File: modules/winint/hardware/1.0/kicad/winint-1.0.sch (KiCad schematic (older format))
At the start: 65 parts, among them J1 Screw_Terminal_01x09, J2 Screw_Terminal_01x09, J3 M12-5PIN, J4 RELAYS, K1 SANYOU_SRD_Form_C, K2 SANYOU_SRD_Form_C, Q1 2N2219, Q2 2N2219, SW1 INSTANCE, U1 ROT, U2 DOK, U3 STP, U4 DEP, U5 RET, U6 OVL, U7 Teensy_3.2, U8 TEC2-2411WI, U9 MCP2551-I-P

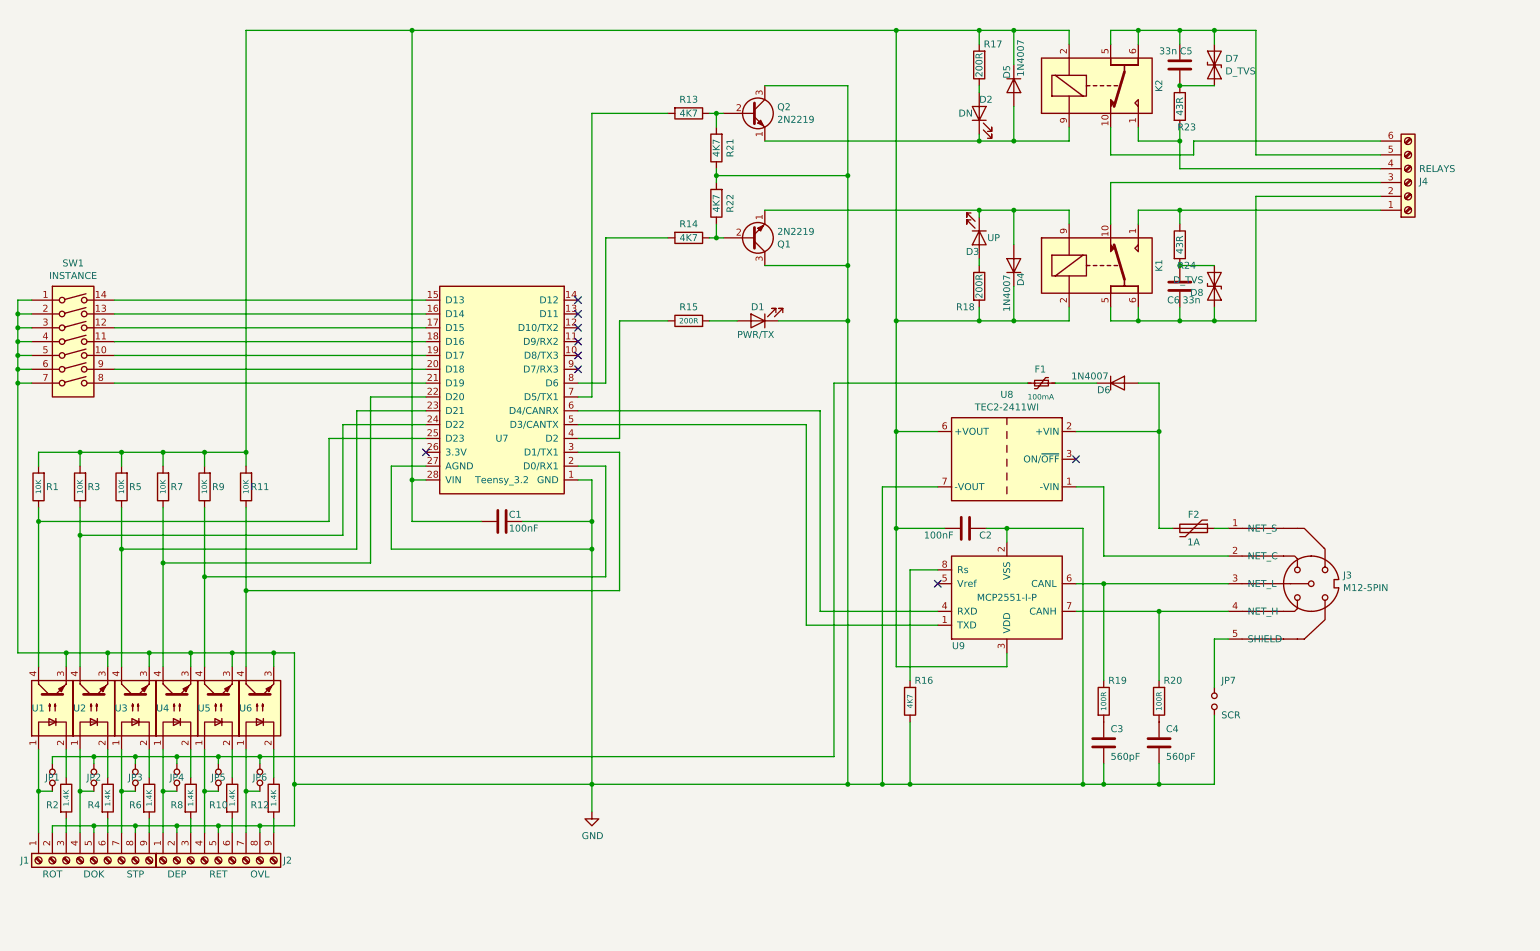
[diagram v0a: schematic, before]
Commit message: Revised PCB layout
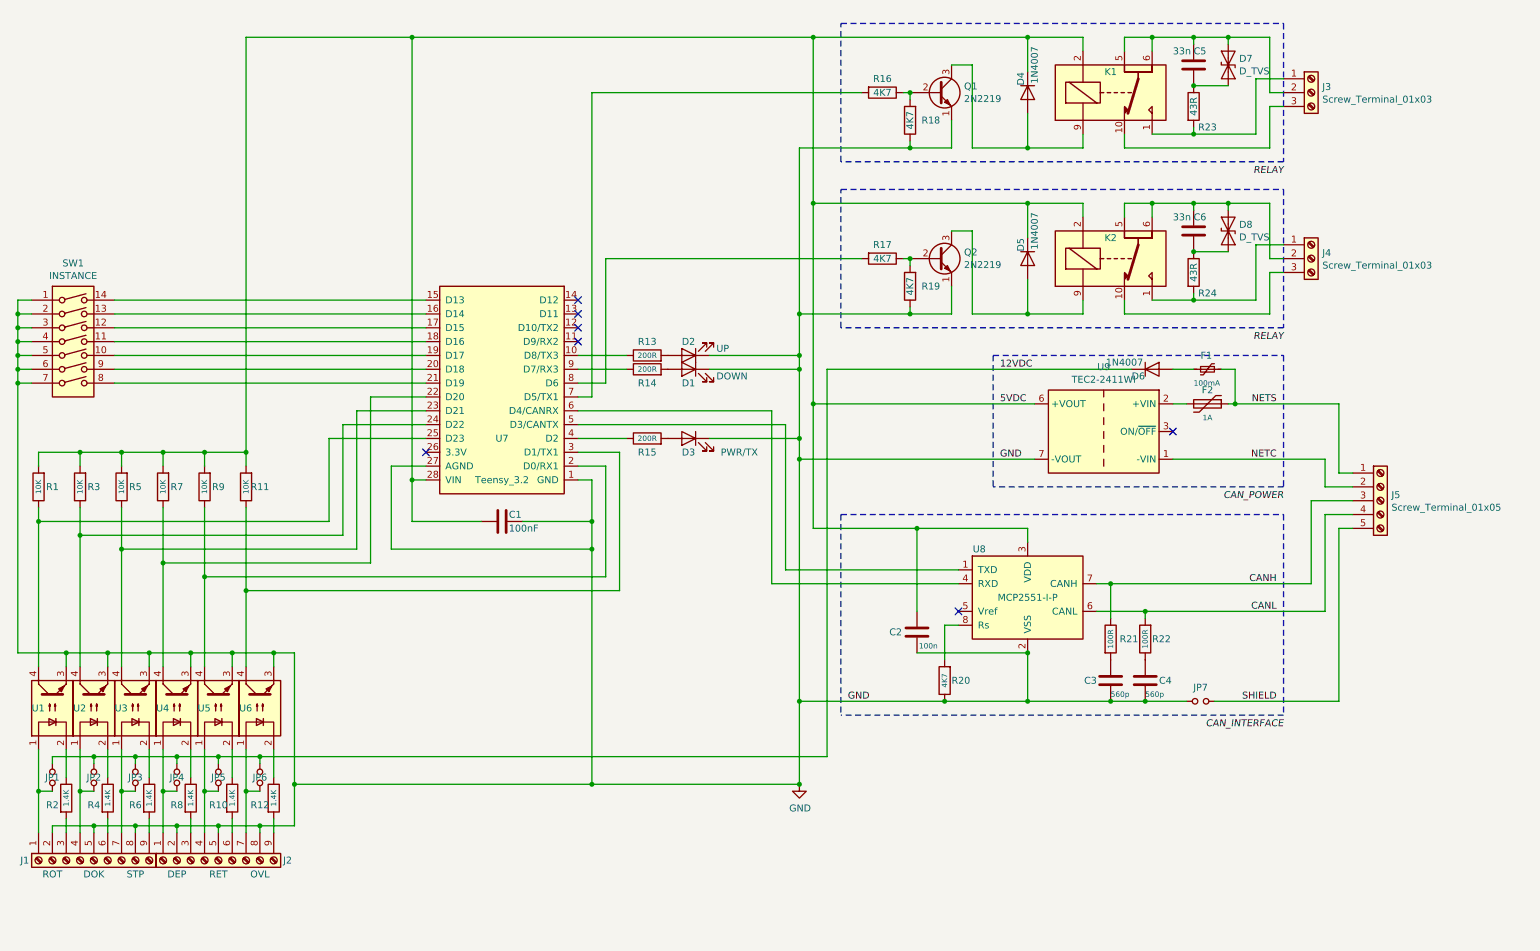
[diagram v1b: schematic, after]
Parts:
- removed D3: UP, LED_THT:LED_D3.0mm, symbol Device:LED
- removed D4: 1N4007, Diode_THT:D_DO-41_SOD81_P7.62mm_Horizontal, symbol Diode:1N4007
- removed J3: M12-5PIN, TerminalBlock_Phoenix:TerminalBlock_Phoenix_MPT-0,5-5-2.54_1x05_P2.54mm_Horizontal, symbol pdjr:M12-5PIN
- removed J4: RELAYS, TerminalBlock_Phoenix:TerminalBlock_Phoenix_MPT-0,5-6-2.54_1x06_P2.54mm_Horizontal, symbol Connector:Screw_Terminal_01x06
- removed R21, R22: 4K7, Resistor_THT:R_Axial_DIN0204_L3.6mm_D1.6mm_P5.08mm_Horizontal, symbol Device:R
- added D1: DOWN, LED_THT:LED_D3.0mm, symbol Device:LED
- added D5: 1N4007, Diode_THT:D_DO-34_SOD68_P2.54mm_Vertical_AnodeUp, symbol Diode:1N4007
- added J3, J4: Screw_Terminal_01x03, TerminalBlock_Phoenix:TerminalBlock_Phoenix_MPT-0,5-3-2.54_1x03_P2.54mm_Horizontal, symbol Connector:Screw_Terminal_01x03
- added J5: Screw_Terminal_01x05, TerminalBlock_Phoenix:TerminalBlock_Phoenix_MPT-0,5-5-2.54_1x05_P2.54mm_Horizontal, symbol Connector:Screw_Terminal_01x05
- added R16, R19: 4K7, Resistor_THT:R_Axial_DIN0204_L3.6mm_D1.6mm_P5.08mm_Horizontal, symbol Device:R
- C2: value 100nF -> 100n
- C3, C4: value 560pF -> 560p
- D2: value DN -> UP
- D4: renamed from D5; footprint Diode_THT:D_DO-41_SOD81_P7.62mm_Horizontal -> Diode_THT:D_DO-34_SOD68_P2.54mm_Vertical_AnodeUp
- K1, K2: footprint PDJR:RS_RELAY_476-757 -> PDJR:476-257
- Q1, Q2: footprint Package_TO_SOT_THT:TO-39-3 -> Package_TO_SOT_THT:TO-18-3
- R13, R14: value 4K7 -> 200R; Power (none) -> 0.125W
- R17, R18: value 200R -> 4K7; Power 0.125W -> (none)
- renumbered D1 to D3, R16 to R20, R19 to R21, R20 to R22, U9 to U8, U8 to U9
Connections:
- net GND: now also D2.1 (K), JP7.2, Q1.1 (E), Q2.1 (E), R18.1, D1.1 (K), R19.1; no longer JP7.1, Q1.3 (C), Q2.3 (C)
- net 5VDC: now reaches C1.1, C2.1, D4.1 (K), K1.2, K2.2, R1.2, R11.2, R3.2, R5.2, R7.2, R9.2, U7.28 (VIN), U8.3 (VDD), U9.6 (+VOUT)
- net 5VDC: now also D5.1 (K); no longer R17.2, R18.2
- net CANH: now reaches R21.1
- net CANH: now also U8.7 (CANH), J5.3 (Pin_3); no longer U8.6 (CANL)
- net CANL: now reaches R22.2
- net CANL: now also U8.6 (CANL), J5.4 (Pin_4); no longer U8.7 (CANH)
- net 12VDC: now reaches D6.1 (K)
- net 12VDC: now also JP1.2, JP2.2, JP3.2, JP4.2, JP5.2, JP6.2; no longer F1.1
- net at K1.9: now also D4.2 (A), Q1.3 (C); no longer Q1.1 (E)
- net at R14.1: now also U7.9 (D7/RX3); no longer Q1.2 (B)
- net at R13.1: now also U7.10 (D8/TX3); no longer Q2.2 (B)
- net at U7.7 (D5/TX1): now also R16.2; no longer R13.2
- net at K1.1: now also R23.2, J3.1 (Pin_1); no longer R24.1
- net at K1.5, K1.6: now also C5.2, D7.1 (A1), J3.2 (Pin_2); no longer C6.2, D8.1 (A1)
- net at K1.10: now also J3.3 (Pin_3)
- net at K2.1: now also R24.2, J4.1 (Pin_1); no longer R23.2
- net at K2.5, K2.6: now also C6.2, D8.1 (A1), J4.2 (Pin_2); no longer C5.2, D7.1 (A1)
- net at K2.10: now also J4.3 (Pin_3)
- net at U7.8 (D6): now also R17.2; no longer R14.2
- net at R17.1: now also Q2.2 (B), R19.2; no longer D2.2 (A)
- net NETS: now reaches F2.1
- net NETS: now also F1.1, J5.1 (Pin_1)
- net at F2.2, U9.2 (+VIN): no longer D6.2 (A)
- net NETC: now reaches U9.1 (-VIN)
- net NETC: now also J5.2 (Pin_2)
- net at C6.1, D8.2 (A2): now also R24.1; no longer R24.2
- new net: D6.2 (A), F1.2
- new net: Q1.2 (B), R16.1, R18.2
- new net: D5.2 (A), K2.9, Q2.3 (C)
- new net: D1.2 (A), R14.2
- new net: D2.2 (A), R13.2
- new net SHIELD: J5.5 (Pin_5), JP7.1
- no-connect marks 9 -> 7
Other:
- moved on the sheet: C2, C3, C4, C5, D3, D4, D6, D7, F1, F2, JP7, R15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

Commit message: Revised PCB layout
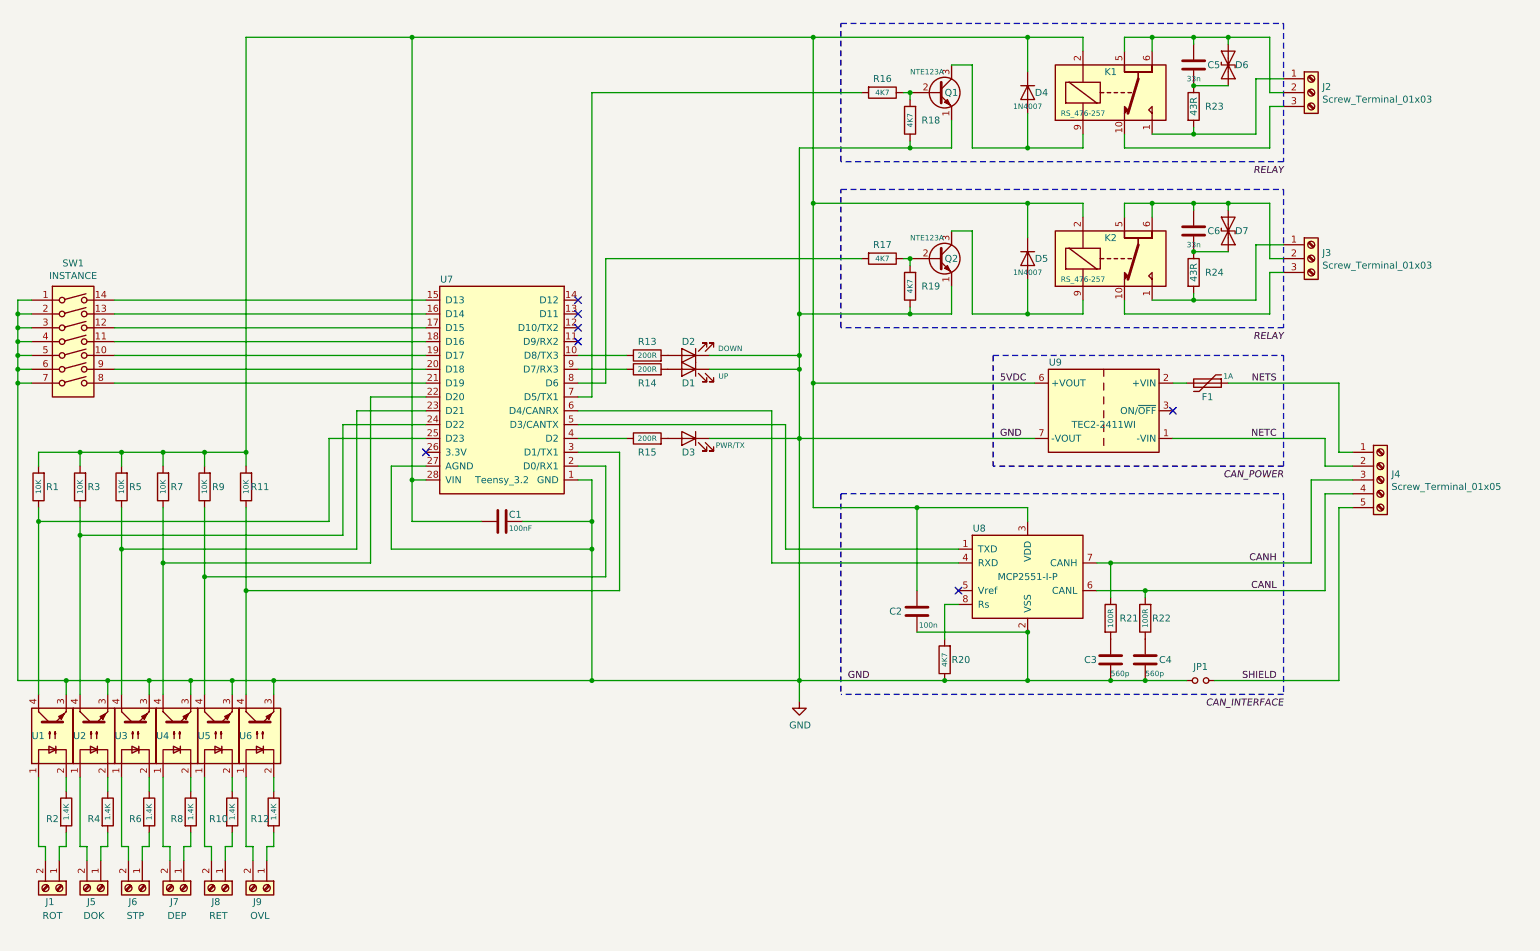
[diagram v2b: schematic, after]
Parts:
- removed D6: 1N4007, Diode_THT:D_DO-41_SOD81_P7.62mm_Horizontal, symbol Diode:1N4007
- removed F1: 100mA, Fuse:Fuse_Littelfuse_395Series, symbol Device:Polyfuse_Small
- removed J1, J2: Screw_Terminal_01x09, TerminalBlock_Phoenix:TerminalBlock_Phoenix_MPT-0,5-9-2.54_1x09_P2.54mm_Horizontal, symbol Connector:Screw_Terminal_01x09
- removed JP1, JP2, JP3, JP4, JP5, JP6: SCR, Connector_PinHeader_2.54mm:PinHeader_1x02_P2.54mm_Vertical, symbol Device:Jumper_NO_Small
- added J1: ROT, TerminalBlock_Phoenix:TerminalBlock_Phoenix_MPT-0,5-2-2.54_1x02_P2.54mm_Horizontal, symbol Connector:Screw_Terminal_01x02
- added J5: DOK, TerminalBlock_Phoenix:TerminalBlock_Phoenix_MPT-0,5-2-2.54_1x02_P2.54mm_Horizontal, symbol Connector:Screw_Terminal_01x02
- added J6: STP, TerminalBlock_Phoenix:TerminalBlock_Phoenix_MPT-0,5-2-2.54_1x02_P2.54mm_Horizontal, symbol Connector:Screw_Terminal_01x02
- added J7: DEP, TerminalBlock_Phoenix:TerminalBlock_Phoenix_MPT-0,5-2-2.54_1x02_P2.54mm_Horizontal, symbol Connector:Screw_Terminal_01x02
- added J8: RET, TerminalBlock_Phoenix:TerminalBlock_Phoenix_MPT-0,5-2-2.54_1x02_P2.54mm_Horizontal, symbol Connector:Screw_Terminal_01x02
- added J9: OVL, TerminalBlock_Phoenix:TerminalBlock_Phoenix_MPT-0,5-2-2.54_1x02_P2.54mm_Horizontal, symbol Connector:Screw_Terminal_01x02
- K1, K2: value SANYOU_SRD_Form_C -> RS_476-257
- Q1, Q2: value 2N2219 -> NTE123A
- renumbered D2 to D1, D1 to D2, D7 to D6, D8 to D7, F2 to F1, J3 to J2, J4 to J3, J5 to J4, JP7 to JP1
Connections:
- net at U1.1: now also J1.2 (Pin_2)
- net at R2.2: now also J1.1 (Pin_1)
- net at U2.1: now also J5.2 (Pin_2)
- net at R4.2: now also J5.1 (Pin_1)
- net at U3.1: now also J6.2 (Pin_2)
- net at R6.2: now also J6.1 (Pin_1)
- net at U4.1: now also J7.2 (Pin_2)
- net at R8.2: now also J7.1 (Pin_1)
- net at U5.1: now also J8.2 (Pin_2)
- net at R10.2: now also J8.1 (Pin_1)
- net at U6.1: now also J9.2 (Pin_2)
- net at R12.2: now also J9.1 (Pin_1)
- net at R14.2: now also D1.2 (A); no longer D2.2 (A)
- net at R13.2: now also D2.2 (A); no longer D1.2 (A)
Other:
- moved on the sheet: C2, C3, C4, D1, D2, F1, J4, JP1, R10, R12, R2, R20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

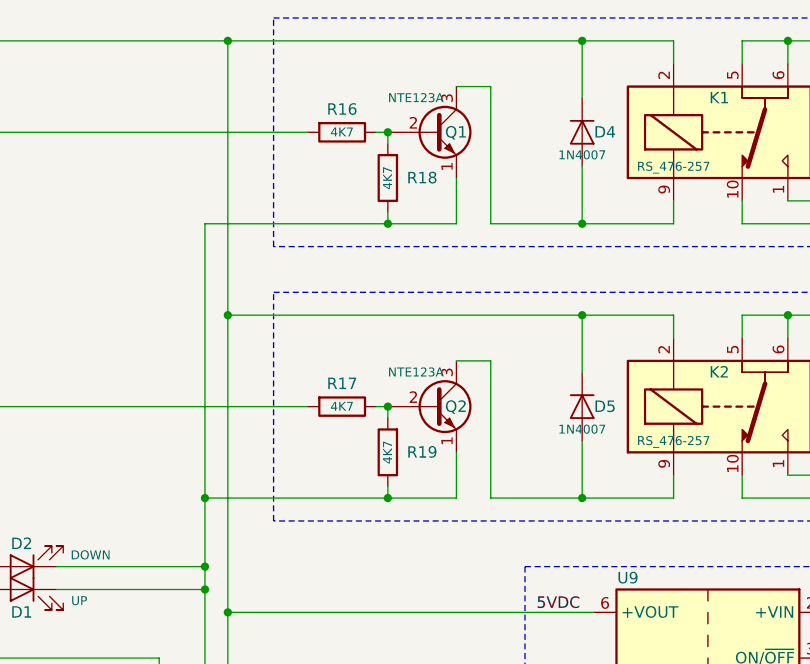
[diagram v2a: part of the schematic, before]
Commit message: Added relat state indicator LEDs
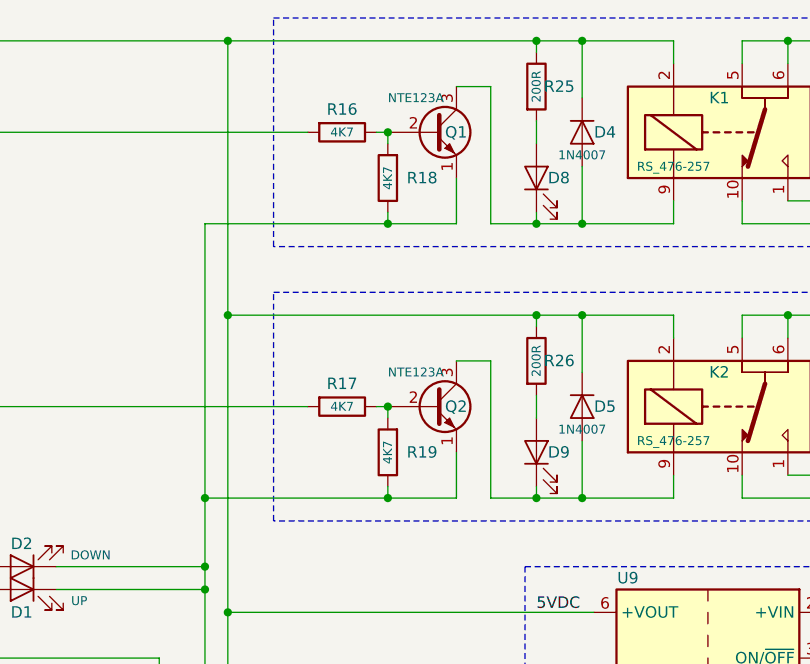
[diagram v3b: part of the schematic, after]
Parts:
- added D8, D9: DOWN, Connector_PinHeader_2.54mm:PinHeader_1x02_P2.54mm_Vertical, symbol Device:LED
- added R25, R26: 200R, Resistor_THT:R_Axial_DIN0204_L3.6mm_D1.6mm_P5.08mm_Horizontal, symbol Device:R
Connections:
- net 5VDC: now also R25.1, R26.1
- net at D4.2 (A), K1.9, Q1.3 (C): now also D8.1 (K)
- net at D5.2 (A), K2.9, Q2.3 (C): now also D9.1 (K)
- new net: D8.2 (A), R25.2
- new net: D9.2 (A), R26.2
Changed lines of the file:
@@
 	8150 5450 8750 5450
 Wire Wire Line
-	6600 800  8150 800
-Wire Wire Line
-	7750 1600 8150 1600
-Wire Wire Line
-	6600 2000 8150 2000
-Wire Wire Line
-	7750 2800 8150 2800
+	6600 800  7950 800
+Wire Wire Line
+	7750 1600 7950 1600
+Wire Wire Line
+	6600 2000 7950 2000
+Wire Wire Line
+	7750 2800 7950 2800
 $Comp
 L Connector:Screw_Terminal_01x03 J2
@@
 Wire Wire Line
 	1300 6150 1300 6650
+$Comp
+L Device:R R25
+U 1 1 5FC0AF39
+P 7950 1000
+F 0 "R25" H 8050 1000 50  0000 C CNN
+F 1 "200R" V 7950 1000 39  0000 C CNN
+F 2 "Resistor_THT:R_Axial_DIN0204_L3.6mm_D1.6mm_P5.08mm_Horizontal" V 7880 1000 50  0001 C CNN
+F 3 "~" H 7950 1000 50  0001 C CNN
+F 4 "0.125W" V 8050 1000 50  0001 C CNN "Power"
+	1    7950 1000
+	1    0    0    -1
+$EndComp
+$Comp
+L Device:LED D8
+U 1 1 5FC0E9ED
+P 7950 1400
+F 0 "D8" V 7950 1350 50  0000 R CNN
+F 1 "DOWN" H 7650 1350 39  0001 C CNN
+F 2 "Connector_PinHeader_2.54mm:PinHeader_1x02_P2.54mm_Vertical" H 7950 1400 50  0001 C CNN
+F 3 "~" H 7950 1400 50  0001 C CNN
+	1    7950 1400
+	0    -1   -1   0
+$EndComp
+Wire Wire Line
+	7950 850  7950 800
+Connection ~ 7950 800
+Wire Wire Line
+	7950 800  8150 800
+Wire Wire Line
+	7950 1550 7950 1600
+Connection ~ 7950 1600
+Wire Wire Line
+	7950 1600 8150 1600
+Wire Wire Line
+	7950 1250 7950 1150
+$Comp
+L Device:R R26
+U 1 1 5FC4BE6B
+P 7950 2200
+F 0 "R26" H 8050 2200 50  0000 C CNN
+F 1 "200R" V 7950 2200 39  0000 C CNN
+F 2 "Resistor_THT:R_Axial_DIN0204_L3.6mm_D1.6mm_P5.08mm_Horizontal" V 7880 2200 50  0001 C CNN
+F 3 "~" H 7950 2200 50  0001 C CNN
+F 4 "0.125W" V 8050 2200 50  0001 C CNN "Power"
+	1    7950 2200
+	1    0    0    -1
+$EndComp
+$Comp
+L Device:LED D9
+U 1 1 5FC4C6ED
+P 7950 2600
+F 0 "D9" V 7950 2550 50  0000 R CNN
+F 1 "DOWN" H 7650 2550 39  0001 C CNN
+F 2 "Connector_PinHeader_2.54mm:PinHeader_1x02_P2.54mm_Vertical" H 7950 2600 50  0001 C CNN
+F 3 "~" H 7950 2600 50  0001 C CNN
+	1    7950 2600
+	0    -1   -1   0
+$EndComp
+Wire Wire Line
+	7950 2050 7950 2000
+Connection ~ 7950 2000
+Wire Wire Line
+	7950 2000 8150 2000
+Wire Wire Line
+	7950 2750 7950 2800
+Connection ~ 7950 2800
+Wire Wire Line
+	7950 2800 8150 2800
+Wire Wire Line
+	7950 2450 7950 2350
 $EndSCHEMATC
